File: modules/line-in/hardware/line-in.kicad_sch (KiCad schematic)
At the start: 37 parts, among them J1 PJ366ST, J10 Eurorack_2x5, J2 PJ301M-12, J3 PJ301M-12, J4 PJ301M-12, U1 TL072CDT, U2 TL072CDT, U3 TL072CDT

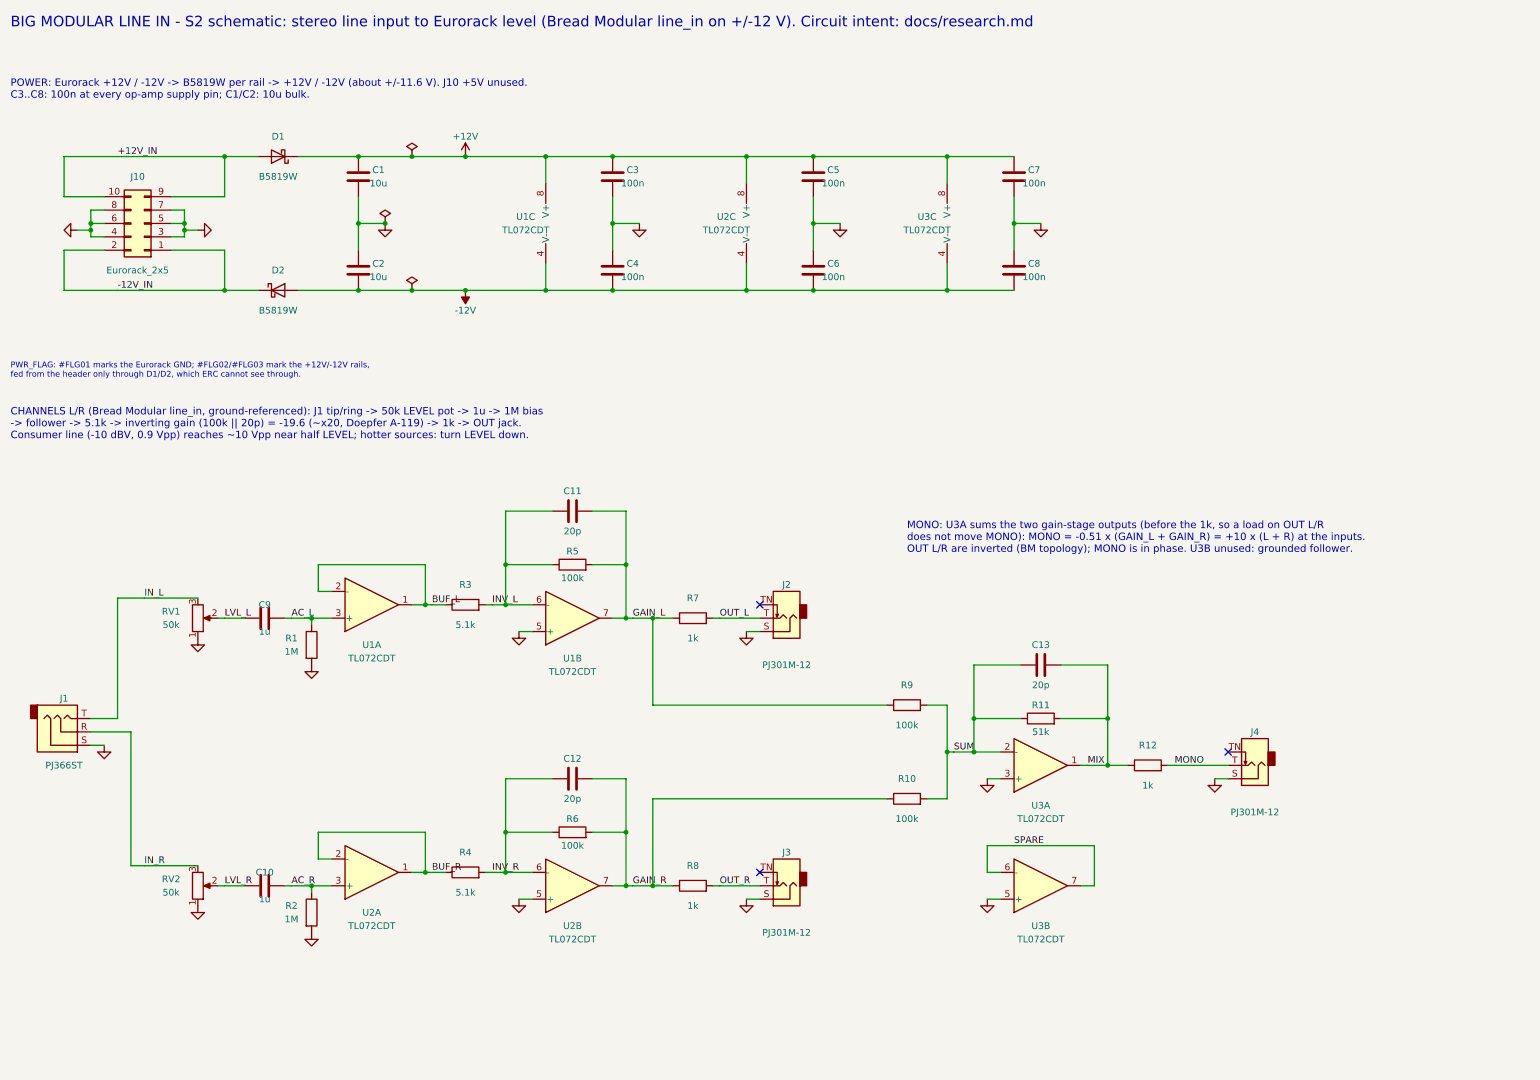
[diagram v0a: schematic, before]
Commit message: Added LINE In Protections.
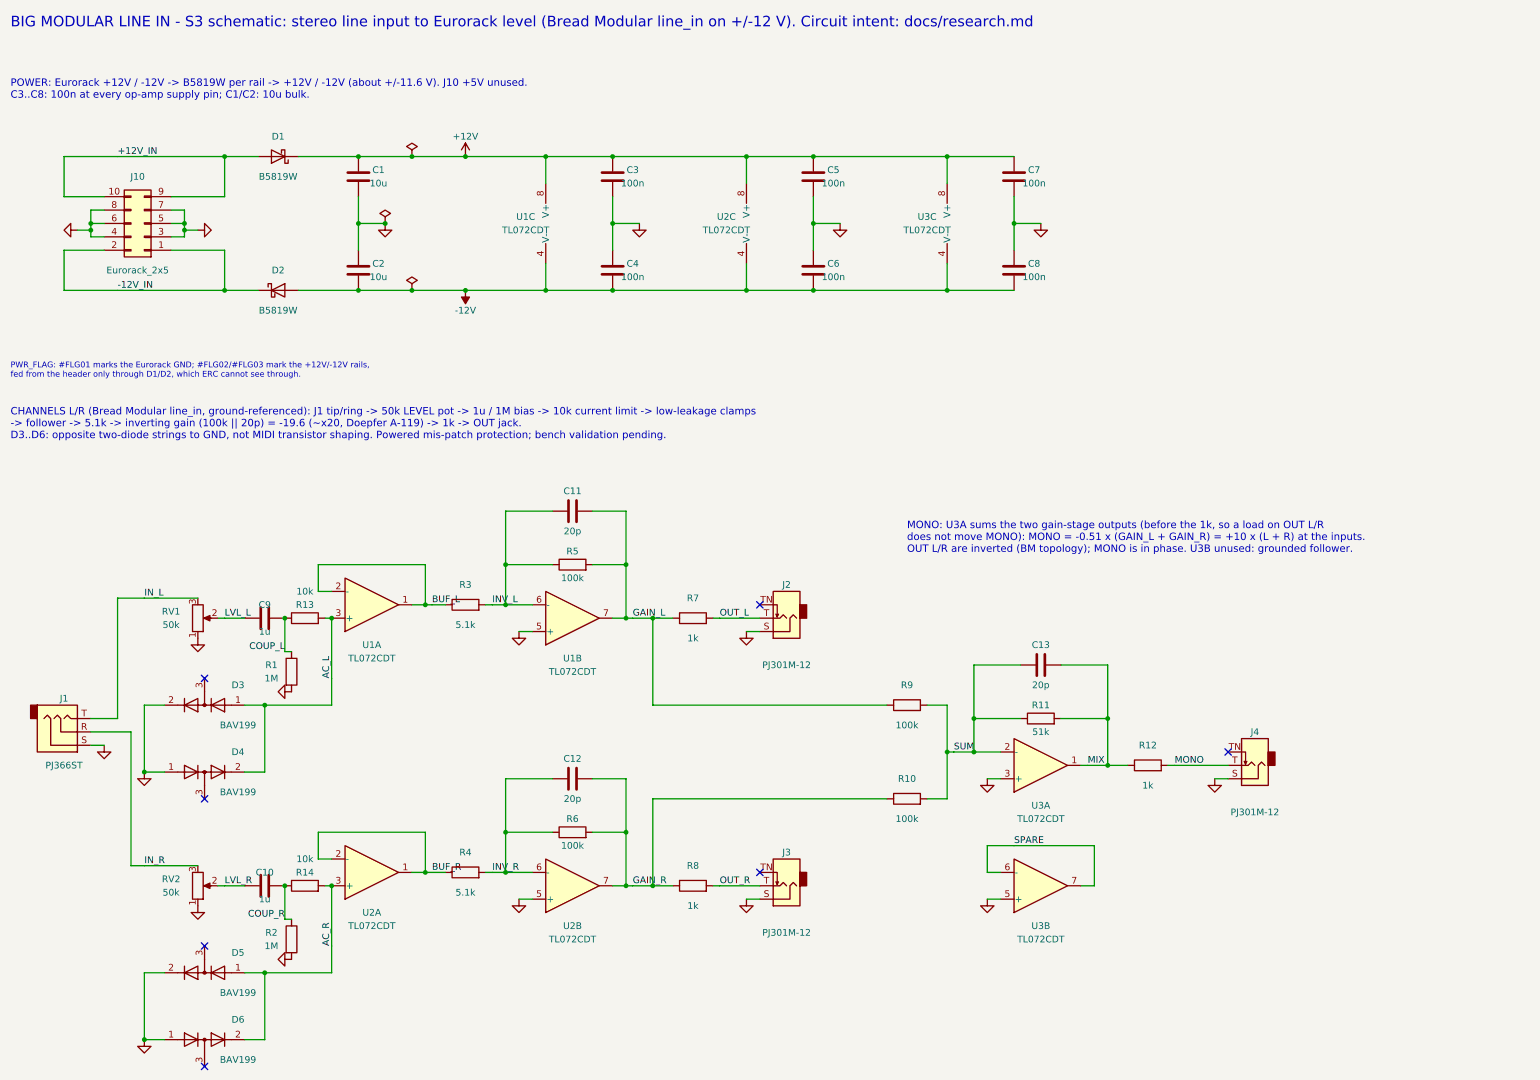
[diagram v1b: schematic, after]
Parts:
- added D3, D4, D5, D6: BAV199, LineIn:SOT-23, symbol LineIn:BAV199
- added R13, R14: 10k, LineIn:R_0603_1608Metric, symbol LineIn:R
- C10, C9: Voltage 25V -> 50V
- R1: Note L follower bias to GND (BM: to V_MID) -> L follower DC bias through R13; on the capacitor side of th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
- R2: Note R follower bias to GND (BM: to V_MID) -> R follower DC bias through R14; on the capacitor side of th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
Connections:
- net AC_L: now also D3.1 (K), D4.2 (A), R13.2; no longer C9.2, R1.1
- net AC_R: now also D5.1 (K), D6.2 (A), R14.2; no longer C10.2, R2.1
- net GND: now also D3.2 (A), D4.1 (K), D5.2 (A), D6.1 (K)
- new net COUP_L: C9.2, R1.1, R13.1
- new net COUP_R: C10.2, R14.1, R2.1
- no-connect marks 3 -> 7
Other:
- note added: "BIG MODULAR LINE IN - S3 schematic: stereo line input to Eurorack level (Bread Modular line_in on +/-12 V). Circuit intent: docs/research.md"
- note added: "CHANNELS L/R (Bread Modular line_in, ground-referenced): J1 tip/ring -> 50k LEVEL pot -> 1u / 1M bias -> 10k current limit -> low-leakage clamps -> follower -> 5.1k -> inverting gain (100k || 20p) = -19.6 (~x20, Doepfer A-119) -> 1k -> OUT jack. D3..D6: opposite two-diode strings to GND, not MIDI transistor shaping. Powered mis-patch protection; bench validation pending."
- note removed: "BIG MODULAR LINE IN - S2 schematic: stereo line input to Eurorack level (Bread Modular line_in on +/-12 V). Circuit intent: docs/research.md"
- note removed: "CHANNELS L/R (Bread Modular line_in, ground-referenced): J1 tip/ring -> 50k LEVEL pot -> 1u -> 1M bias -> follower -> 5.1k -> inverting gain (100k || 20p) = -19.6 (~x20, Doepfer A-119) -> 1k -> OUT jack. Consumer line (-10 dBV, 0.9 Vpp) reaches ~10 Vpp near half LEVEL; hotter sources: turn LEVEL down."
- moved on the sheet: R1, R2
